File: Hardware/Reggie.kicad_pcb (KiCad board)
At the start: 4 copper layers, 79.5 x 65.8 mm, 220 parts, among them IC1 ADS131M04IRUKR, IC2 TPS61089RNRR, IC3 AP2205-W5-7, IC4 AP2205-W5-7, IC5 TPS61089RNRR, J1 RBUS, J2 USB_C_Receptacle_USB2.0, J3 ServoConnector1, J4 1053131104, J5 1053131104, J6 1053131104, J7 ST1W008S4TR2000, Q1 SSM3K15AMFV,L3F, Q2 PMOS, U1 ESP32-S3, U2 SN65HVD230, U3 LM66200DRLR, U4 MAX77827AEFD+T, U5 SC4215ASTRT, U6 MAX31856, U7 MAX31856, U8 SiC437AED-T1, Y1 R940000171

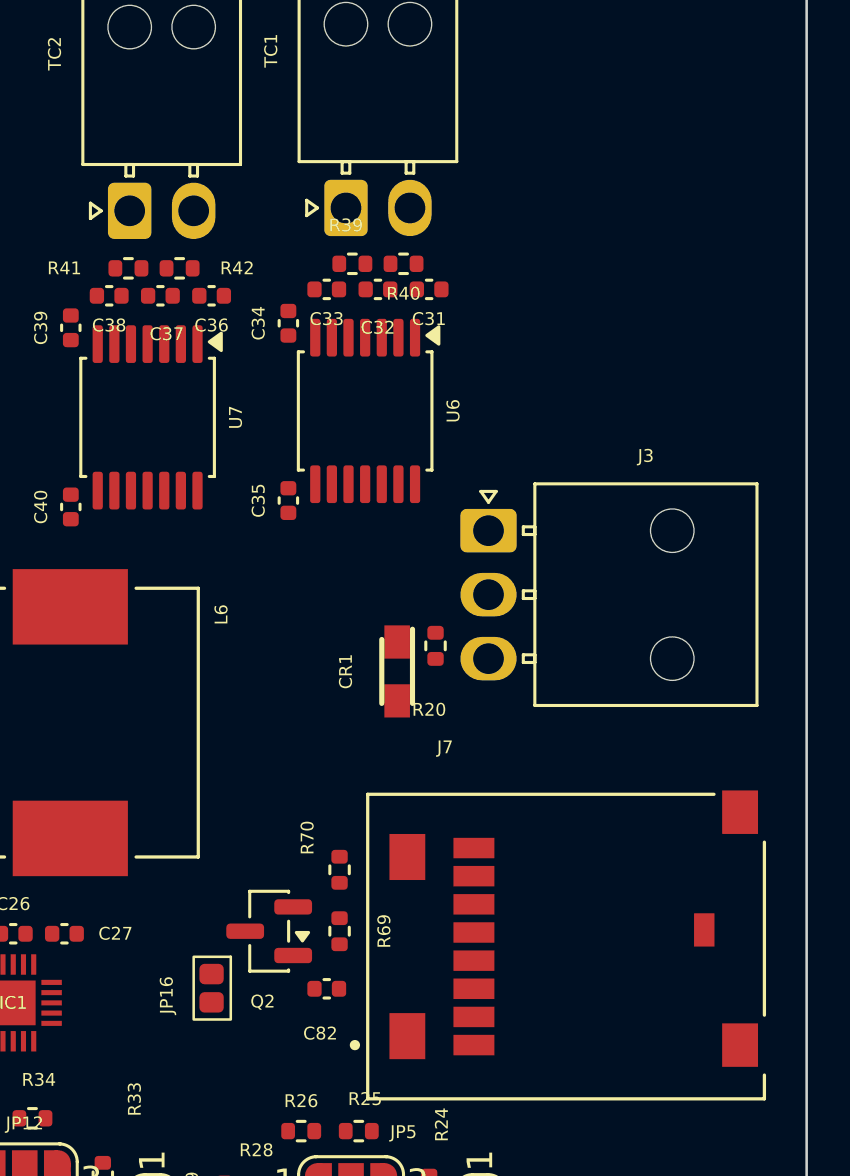
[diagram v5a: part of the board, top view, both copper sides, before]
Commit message: schematic changes and updated tvs footprints
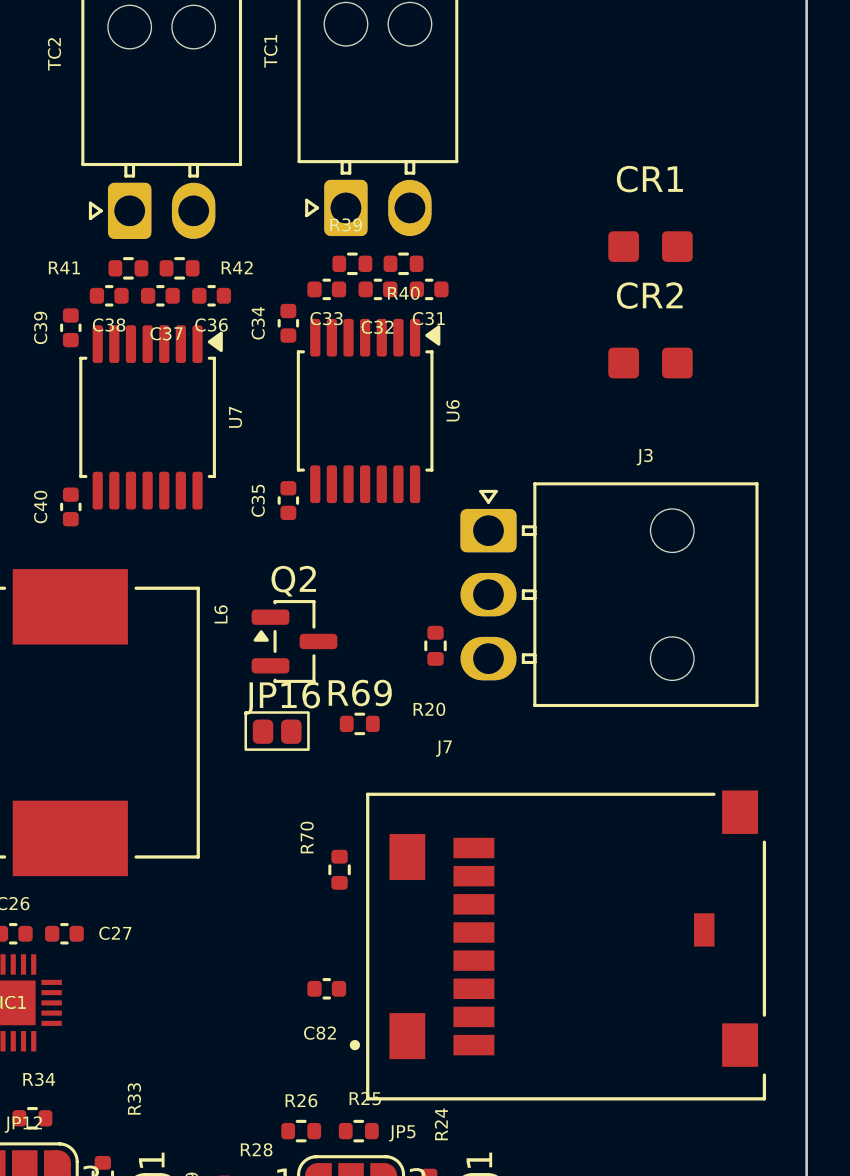
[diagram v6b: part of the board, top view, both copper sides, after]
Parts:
- added CR2: CPDF5V0U-HF, iclr:CPD, F.Cu at (185.1, 72.8)
- CR1: footprint Diode_SMD:DIOM2512X90N -> iclr:CPD
- R9: value R -> 18k
- moved CR1 19.3 mm to (185.1, 68.2), turned to 0 degrees
- moved Q2 11.4 mm to (171.2, 83.7), turned to 0 degrees
- moved JP16 10.7 mm to (170.8, 87.2), turned to 0 degrees
- moved R69 8.14 mm to (173.7, 86.9), turned to 0 degrees
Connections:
- net /Ldo/FB_12V renamed /Sensor Power/FB_12V
- net /Ldo/FB_5V renamed /Sensor Power/FB_5V
- net /Ldo/LDO12V_IN renamed /Sensor Power/LDO12V_IN
- net /Ldo/LDO5.5V_IN renamed /Sensor Power/LDO5.5V_IN
- net /Ldo/SW_12V renamed /Sensor Power/SW_12V
- net /Ldo/SW_5V renamed /Sensor Power/SW_5V
- C58 pad 1: /Ldo/12V -> +12V
- C82 pad 1: +3V3 -> Net-(JP16-B)
- CR1 pad 1: /Servo/ServoPWM -> GND
- CR1 pad 2: GND -> /Servo/ServoPWM
- IC1 pad 12: /VSPI_SCLK -> /HSPI_SCLK
- IC1 pad 13: /VSPI_MISO -> /HSPI_MISO
- IC1 pad 14: /VSPI_MOSI -> /HSPI_MOSI
- IC4 pad 5: /Ldo/12V -> +12V
- J7 pad C2: /SD1_CS -> /SD_CS
- J7 pad C4: +3V3 -> Net-(JP16-B)
- R55 pad 2: /Ldo/12V -> +12V
- R69 pad 2: +3V3 -> /SD_EN
- U1 pad 14: unconnected-(U1-GPIO9/ADC1_CH8-Pad14) -> /ServoPWM
- U1 pad 15: unconnected-(U1-GPIO10/ADC1_CH9-Pad15) -> /SD_EN
- U1 pad 16: unconnected-(U1-GPIO11/ADC2_CH0-Pad16) -> /SD_DET
- U1 pad 17: unconnected-(U1-GPIO12/ADC2_CH1-Pad17) -> /SD_CS
- U1 pad 38: /ServoPWM -> /HSPI_MOSI
- U1 pad 39: /VSPI_MOSI -> /HSPI_MISO
- U1 pad 40: /VSPI_MISO -> /HSPI_SCLK
- U1 pad 41: /VSPI_SCLK -> /VSPI_MOSI
- U1 pad 42: /SD1_CS -> /VSPI_SCLK
- U1 pad 43: /SD_DET -> /VSPI_MISO
- U1 pad 51: +3V3 -> unconnected-(U1-GPIO45-Pad51)
- U6 pad 10: /VSPI_SCLK -> /HSPI_SCLK
- U6 pad 11: /VSPI_MISO -> /HSPI_MISO
- U6 pad 12: /VSPI_MOSI -> /HSPI_MOSI
- U7 pad 10: /VSPI_SCLK -> /HSPI_SCLK
- U7 pad 11: /VSPI_MISO -> /HSPI_MISO
- U7 pad 12: /VSPI_MOSI -> /HSPI_MOSI

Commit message: Overall Packing Complete!!
Version1
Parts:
- moved H4 200.9 mm to (186.5, 106.5)
- moved H3 189.1 mm to (186.5, 63.5)
- moved H2 154.2 mm to (123.5, 106.5)
- moved TP6 135.6 mm to (160.5, 74.6)
- moved H1 134.7 mm to (123.5, 63.5)
- moved TP7 120.1 mm to (136.3, 91.2)
- moved TP5 109.5 mm to (121.7, 86.4)
- moved TP8 105.2 mm to (128.3, 78.8)
- moved C53 76.8 mm to (183.7, 81.6)
- moved C54 76.8 mm to (177.7, 75.1)
- moved C55 76.8 mm to (178.2, 77.3)
- moved C56 76.8 mm to (176.7, 77.8)
- moved C57 76.8 mm to (180.2, 80.8)
- moved C58 76.8 mm to (189.7, 81.1)
- moved C59 76.8 mm to (182.2, 80.8)
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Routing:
- net +3V3: track 0.00 -> 28.6 mm
- net /CAN-: track 0.00 -> 14.9 mm
- net /Data+: track 0.00 -> 11.2 mm
- net /CHIP_PU: track 0.00 -> 10.7 mm
- net /BOOT: track 0.00 -> 9.71 mm
- net /CAN+: track 0.00 -> 7.68 mm
- net Net-(C13-Pad1): track 0.00 -> 6.92 mm
- net Net-(JP4-C): track 0.00 -> 6.31 mm
- net Net-(JP12-C): track 0.00 -> 6.16 mm
- net Net-(JP5-C): track 0.00 -> 6.16 mm
- net /RXD: track 0.00 -> 6.09 mm
- net /TXD: track 0.00 -> 5.59 mm
- net Net-(U1-XTAL_N): track 0.00 -> 5.09 mm
- net Net-(JP11-C): track 0.00 -> 4.96 mm
- net /Data-: track 0.00 -> 4.81 mm
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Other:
- board size 79.5 x 65.8 mm -> 70 x 50 mm

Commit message: Overall Packing Backup Version
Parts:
- added D6: RCLAMP3346PQTNT, iclr:RCLAMP3346PQTNT, F.Cu at (138.2, 85.4)
- added J8: GPIO Breakout, Connector_PinSocket_2.54mm:PinSocket_2x04_P2.54mm_Vertical, F.Cu at (126.6, 94.0)
- moved C76 88.2 mm to (87.3, 135.5)
- moved C77 88.2 mm to (95.5, 147.2)
- moved C78 88.2 mm to (87.3, 138.9)
- moved C80 88.2 mm to (87.3, 145.6)
- moved C81 88.2 mm to (87.3, 148.9)
- moved C79 88.2 mm to (87.3, 142.2)
- moved J3 60.3 mm to (185.3, 82.4), turned to 0 degrees
- moved R70 58.7 mm to (130.1, 99.0), turned to 90 degrees
- moved R20 56.8 mm to (183.0, 84.6)
- moved CR1 56.2 mm to (183.0, 87.9), turned to -90 degrees
- moved TP7 50.3 mm to (91.7, 114.4)
- moved J7 45.4 mm to (139.7, 101.9), turned to -90 degrees
- moved J2 44.2 mm to (153.5, 60.9), turned to 180 degrees
- moved IC4 39.0 mm to (149.7, 95.7)
- moved R14 38.7 mm to (151.3, 65.0), turned to 0 degrees
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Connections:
- CR1 pad 2: /Servo/ServoPWM -> /ServoPWM
- R20 pad 1: /Servo/ServoPWM -> /ServoPWM
- U1 pad 18: unconnected-(U1-GPIO13/ADC2_CH2-Pad18) -> /GPIO13
- U1 pad 19: unconnected-(U1-GPIO14/ADC2_CH3-Pad19) -> /GPIO14
- U1 pad 21: unconnected-(U1-GPIO15/ADC2_CH4/XTAL_32K_P-Pad21) -> /GPIO15
- U1 pad 22: unconnected-(U1-GPIO16/ADC2_CH5/XTAL_32K_N-Pad22) -> /GPIO16
- U1 pad 44: unconnected-(U1-MTCK/JTAG/GPIO39-Pad44) -> /GPIO39
- U1 pad 9: unconnected-(U1-GPIO4/ADC1_CH3-Pad9) -> /GPIO4
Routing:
- net /T_DRDY0: track 0.00 -> 19.4 mm
- net +3V3: track 28.6 -> 38.6 mm
- net Net-(JP16-B): track 0.00 -> 9.13 mm
- net Net-(TC2--): track 0.00 -> 8.28 mm
- net Net-(TC1--): track 0.00 -> 7.64 mm
- net /RXD: track 6.09 -> 0.00 mm
- net Net-(U7-T-): track 0.00 -> 4.16 mm
- net Net-(U7-T+): track 0.00 -> 4.04 mm
- net /BOOT: track 9.71 -> 13.7 mm
- net Net-(U6-T-): track 0.00 -> 3.92 mm
- net Net-(U6-T+): track 0.00 -> 3.80 mm
- net Net-(TC2-+): track 0.00 -> 2.48 mm
- net Net-(TC1-+): track 0.00 -> 2.29 mm
- net Net-(C13-Pad1): track 6.92 -> 4.81 mm
- net (no net): vias 0 -> 7
